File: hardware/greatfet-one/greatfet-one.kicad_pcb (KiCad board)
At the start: 4 copper layers, 70.6 x 53.3 mm, 88 parts, among them J1 NEIGHBOR1, J2 NEIGHBOR2, J3 USB-MICRO-B-SHIELDED, J4 USB-MICRO-B-SHIELDED, J5 JTAG, J7 BONUS_ROW, SW1 DFU, SW2 RESET, U1 LPC4330FBD144, U2 W25Q16DV, U3 AP7333, U4 IP4220CZ6, U5 NX5P2553GV, X1 XTAL4PIN, X2 RTC_XTAL

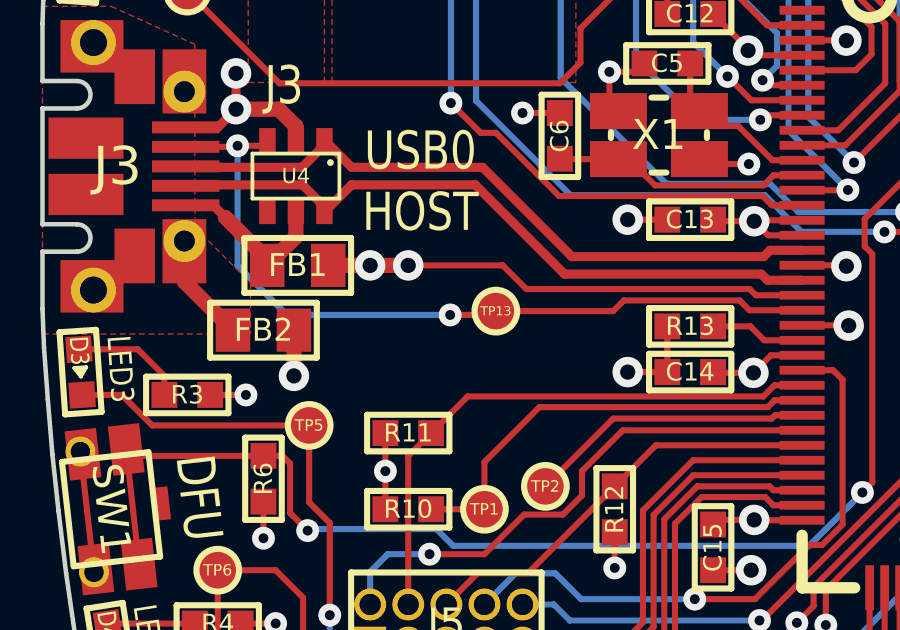
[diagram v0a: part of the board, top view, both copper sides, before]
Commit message: GreatFET One: updated layout to reflect VBUS changes
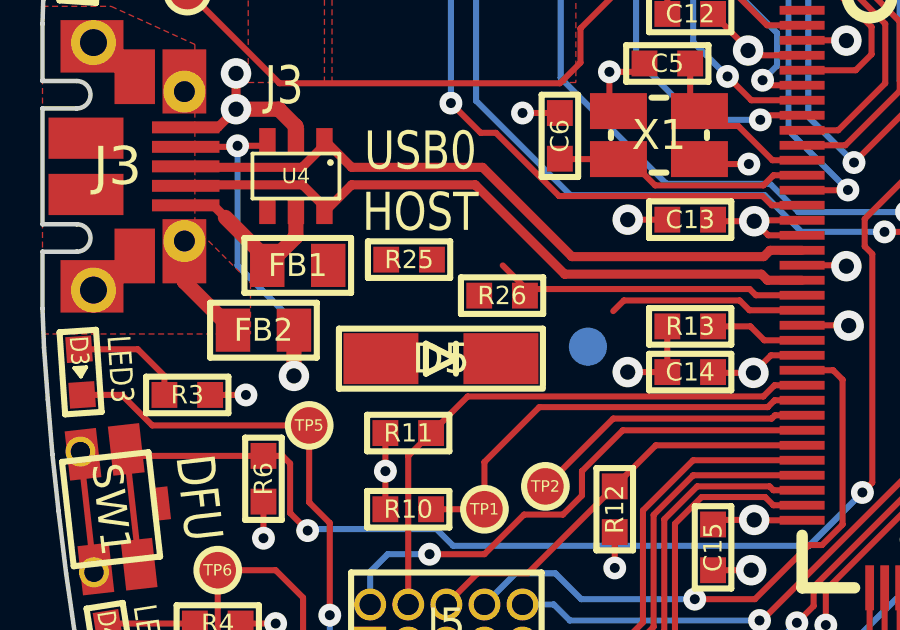
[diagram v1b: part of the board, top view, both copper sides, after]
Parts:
- added D5: VBUS_DIODE, gsg-modules:B140-13-F, F.Cu at (119.2, 104.2)
- added R25: 10k, gsg-modules:0603, F.Cu at (118.1, 100.9)
- added R26: 18k, gsg-modules:0603, F.Cu at (121.2, 102.1)
- R22: value 12.0k -> 18k
- TP13: moved to B.Cu
- X1: value XTAL4PIN -> MCU_XTAL
- moved TP13 3.29 mm to (124.1, 103.8)
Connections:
- net Net-(FB1-Pad1) renamed /USB0_VBUS
- C10 pad 1: /VBUS -> +5V
- C4 pad 1: /VBUS -> +5V
- FB1 pad 2: /VBUS -> Net-(D5-Pad2)
- J2 pad 2: /VBUS -> +5V
- U1 pad 21: /VBUS -> /USB0_SENSE
- U3 pad 1: /VBUS -> +5V
- U5 pad 1: /VBUS -> +5V
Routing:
- net /VBUS: track 21.2 -> 0.00 mm, vias 5 -> 0
- net /USB0_ID: track 26.6 -> 15.7 mm, vias 2 -> 1
- net /USB0_SENSE: track 0.00 -> 10.4 mm
- net +5V: track 0.00 -> 5.05 mm, vias 0 -> 3
- added copper zone on B.Cu, net +5V
- added copper zone on F.Cu, net +5V
- removed copper zone on B.Cu, net /VBUS
- removed copper zone on F.Cu, net /VBUS

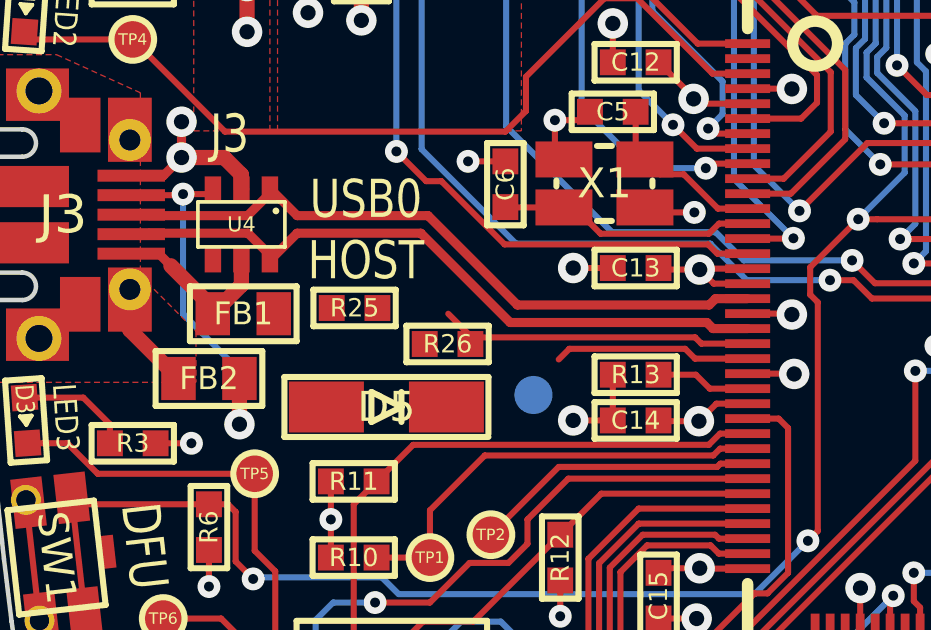
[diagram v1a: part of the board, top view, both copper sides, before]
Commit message: GreatFET One: changed U5 from NX5P2553GVH (end of life) to AP2553W6-7, updated ILIM resistor R23
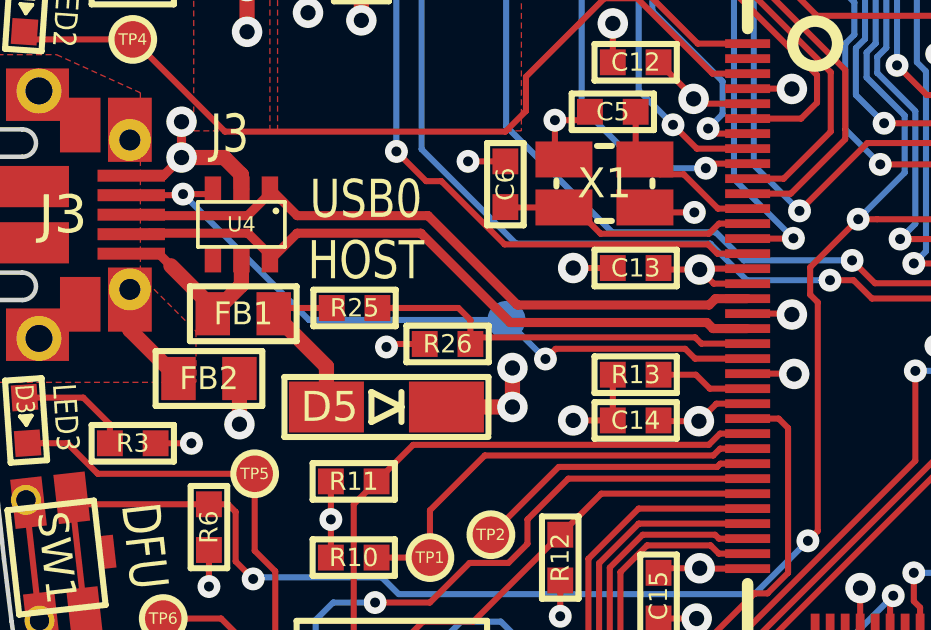
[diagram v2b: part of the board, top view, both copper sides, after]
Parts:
- R23: value 49.9k -> 43.2k
- U5: value NX5P2553GV -> AP2553W6-7
- moved TP13 2.66 mm to (123.2, 101.3)
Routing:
- net /USB0_ID: track 15.7 -> 24.2 mm, vias 1 -> 2
- net Net-(D5-Pad2): track 0.00 -> 5.85 mm
- net +5V: track 5.05 -> 8.55 mm, vias 3 -> 5
- net /USB0_SENSE: track 10.4 -> 13.5 mm
- net GND: track 80.9 -> 82.2 mm, vias 46 -> 47
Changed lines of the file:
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@@
   (general
     (links 356)
-    (no_connects 10)
-    (area 93.271704 68.58 207.466001 199.465001)
+    (no_connects 0)
+    (area 105.842999 71.044999 176.605001 124.535001)
     (thickness 1.6)
     (drawings 154)
-    (tracks 1422)
+    (tracks 1438)
     (zones 0)
     (modules 91)
@@
       (effects (font (size 0.508 0.508) (thickness 0.127)))
     )
-    (fp_text value NX5P2553GV (at 0 0 180) (layer F.SilkS) hide
+    (fp_text value AP2553W6-7 (at 0 0 180) (layer F.SilkS) hide
       (effects (font (size 0.762 0.889) (thickness 0.1905)))
     )
@@
       (effects (font (size 0.6096 0.6096) (thickness 0.1524)))
     )
-    (fp_text value 49.9k (at 0 0) (layer F.SilkS) hide
+    (fp_text value 43.2k (at 0 0) (layer F.SilkS) hide
       (effects (font (size 0.6096 0.6096) (thickness 0.1524)))
     )
@@
   )
   (module gsg-modules:TESTPOINT-50MIL (layer B.Cu)
-    (at 124.1 103.8)
+    (at 123.2 101.3)
     (fp_text reference TP13 (at 0 0) (layer B.SilkS)
       (effects (font (size 0.3048 0.3048) (thickness 0.0762)) (justify mirror))
@@
   (module gsg-modules:B140-13-F placed (layer F.Cu)
     (at 119.2 104.2 180)
-    (fp_text reference D5 (at 0 0 360) (layer F.SilkS)
+    (fp_text reference D5 (at 1.9 0 360) (layer F.SilkS)
       (effects (font (size 1 1) (thickness 0.15)))
     )
@@
   (gr_line (start 172.72 124.46) (end 112.3188 124.46) (angle 90) (layer Edge.Cuts) (width 0.15))
   (gr_line (start 112.3188 71.12) (end 172.72 71.12) (angle 90) (layer Edge.Cuts) (width 0.15))
+  (segment (start 120.476 102.1) (end 119.3 102.1) (width 0.2032) (layer F.Cu) (net 1))
+  (via (at 119.2 102.2) (size 0.762) (drill 0.3302) (layers F.Cu B.Cu) (net 1))
+  (segment (start 119.3 102.1) (end 119.2 102.2) (width 0.2032) (layer F.Cu) (net 1))
   (segment (start 123.1646 96.012) (end 121.92 96.012) (width 0.2032) (layer F.Cu) (net 1))
   (via (at 121.92 96.012) (size 0.762) (drill 0.3302) (layers F.Cu B.Cu) (net 1))
@@
   (segment (start 167.894 75.184) (end 167.894 76.708) (width 0.2032) (layer F.Cu) (net 91))
   (segment (start 166.37 73.66) (end 167.894 75.184) (width 0.2032) (layer F.Cu) (net 91) (status 10))
-  (segment (start 125.2982 102.2604) (end 124.9426 102.616) (width 0.2032) (layer F.Cu) (net 92))
-  (segment (start 129.159 102.2604) (end 125.2982 102.2604) (width 0.2032) (layer F.Cu) (net 92))
-  (segment (start 129.48666 102.58806) (end 129.159 102.2604) (width 0.2032) (layer F.Cu) (net 92))
+  (segment (start 116.6162 101.3) (end 112.4204 97.1042) (width 0.2032) (layer B.Cu) (net 92))
+  (segment (start 129.159 102.2604) (end 124.8396 102.2604) (width 0.2032) (layer F.Cu) (net 92))
   (segment (start 131.23926 102.58806) (end 129.48666 102.58806) (width 0.2032) (layer F.Cu) (net 92))
-  (segment (start 114.061238 102.743) (end 112.4204 101.102162) (width 0.2032) (layer B.Cu) (net 92))
+  (segment (start 129.48666 102.58806) (end 129.159 102.2604) (width 0.2032) (layer F.Cu) (net 92))
+  (segment (start 123.2 101.3) (end 116.6162 101.3) (width 0.2032) (layer B.Cu) (net 92))
+  (segment (start 124.5 102.6) (end 123.2 101.3) (width 0.2032) (layer B.Cu) (net 92))
+  (via (at 124.5 102.6) (size 0.762) (drill 0.3302) (layers F.Cu B.Cu) (net 92))
+  (segment (start 124.8396 102.2604) (end 124.5 102.6) (width 0.2032) (layer F.Cu) (net 92))
   (via (at 112.4204 97.1042) (size 0.762) (drill 0.3302) (layers F.Cu B.Cu) (net 92))
-  (segment (start 112.4204 101.102162) (end 112.4204 97.1042) (width 0.2032) (layer B.Cu) (net 92))
   (segment (start 113.2258 97.1042) (end 112.4204 97.1042) (width 0.2032) (layer F.Cu) (net 92))
   (segment (start 112.3846 97.14) (end 112.4204 97.1042) (width 0.2032) (layer F.Cu) (net 92))
@@
   (segment (start 170.688 103.759) (end 172.657 101.79) (width 0.508) (layer F.Cu) (net 136))
   (segment (start 172.657 101.79) (end 172.9924 101.79) (width 0.508) (layer F.Cu) (net 136))
+  (segment (start 123.4 102.9) (end 123.4 104.2) (width 0.508) (layer F.Cu) (net 137))
+  (segment (start 123.4 104.2) (end 121.2 104.2) (width 0.508) (layer F.Cu) (net 137))
+  (via (at 123.4 104.2) (size 1.016) (drill 0.508) (layers F.Cu B.Cu) (net 137))
+  (via (at 123.4 102.9) (size 1.016) (drill 0.508) (layers F.Cu B.Cu) (net 137))
   (segment (start 116.586 89.789) (end 116.586 91.059) (width 0.508) (layer F.Cu) (net 137))
   (via (at 116.586 91.059) (size 1.016) (drill 0.508) (layers F.Cu B.Cu) (net 137))
@@
   (segment (start 171.13 86.426) (end 171.196 86.36) (width 0.3048) (layer F.Cu) (net 137))
   (via (at 171.196 86.36) (size 1.016) (drill 0.508) (layers F.Cu B.Cu) (net 137))
+  (segment (start 117.2 104.2) (end 117.2 102.849) (width 0.508) (layer F.Cu) (net 138))
+  (segment (start 117.2 102.849) (end 115.443 101.092) (width 0.508) (layer F.Cu) (net 138))
+  (segment (start 117.376 100.9) (end 115.635 100.9) (width 0.2032) (layer F.Cu) (net 138))
+  (segment (start 115.635 100.9) (end 115.443 101.092) (width 0.2032) (layer F.Cu) (net 138))
   (segment (start 113.411 100.8888) (end 113.411 101.092) (width 0.508) (layer F.Cu) (net 139))
   (segment (start 113.411 100.8888) (end 112.014 99.4918) (width 0.508) (layer F.Cu) (net 139))
@@
   (segment (start 113.411 101.092) (end 114.366 100.137) (width 0.508) (layer F.Cu) (net 139))
   (segment (start 114.366 100.137) (end 114.366 99.314) (width 0.508) (layer F.Cu) (net 139))
-  (segment (start 122.047 101.8794) (end 121.2596 101.092) (width 0.2032) (layer F.Cu) (net 140))
-  (segment (start 129.4892 101.8794) (end 122.047 101.8794) (width 0.2032) (layer F.Cu) (net 140))
+  (segment (start 122.2206 101.8794) (end 122 102.1) (width 0.2032) (layer F.Cu) (net 140))
+  (segment (start 118.9 100.9) (end 121.6 100.9) (width 0.2032) (layer F.Cu) (net 140))
+  (segment (start 122 101.3) (end 122 102.1) (width 0.2032) (layer F.Cu) (net 140))
+  (segment (start 121.6 100.9) (end 122 101.3) (width 0.2032) (layer F.Cu) (net 140))
+  (segment (start 122.2206 101.8794) (end 129.4892 101.8794) (width 0.2032) (layer F.Cu) (net 140))
+  (segment (start 129.69748 102.08768) (end 131.23926 102.08768) (width 0.2032) (layer F.Cu) (net 140))
   (segment (start 129.69748 102.08768) (end 129.4892 101.8794) (width 0.2032) (layer F.Cu) (net 140))
-  (segment (start 131.23926 102.08768) (end 129.69748 102.08768) (width 0.2032) (layer F.Cu) (net 140))
   (zone (net 1) (net_name GND) (layer C2.Cu) (hatch edge 0.508)
     (connect_pads (clearance 0.254))

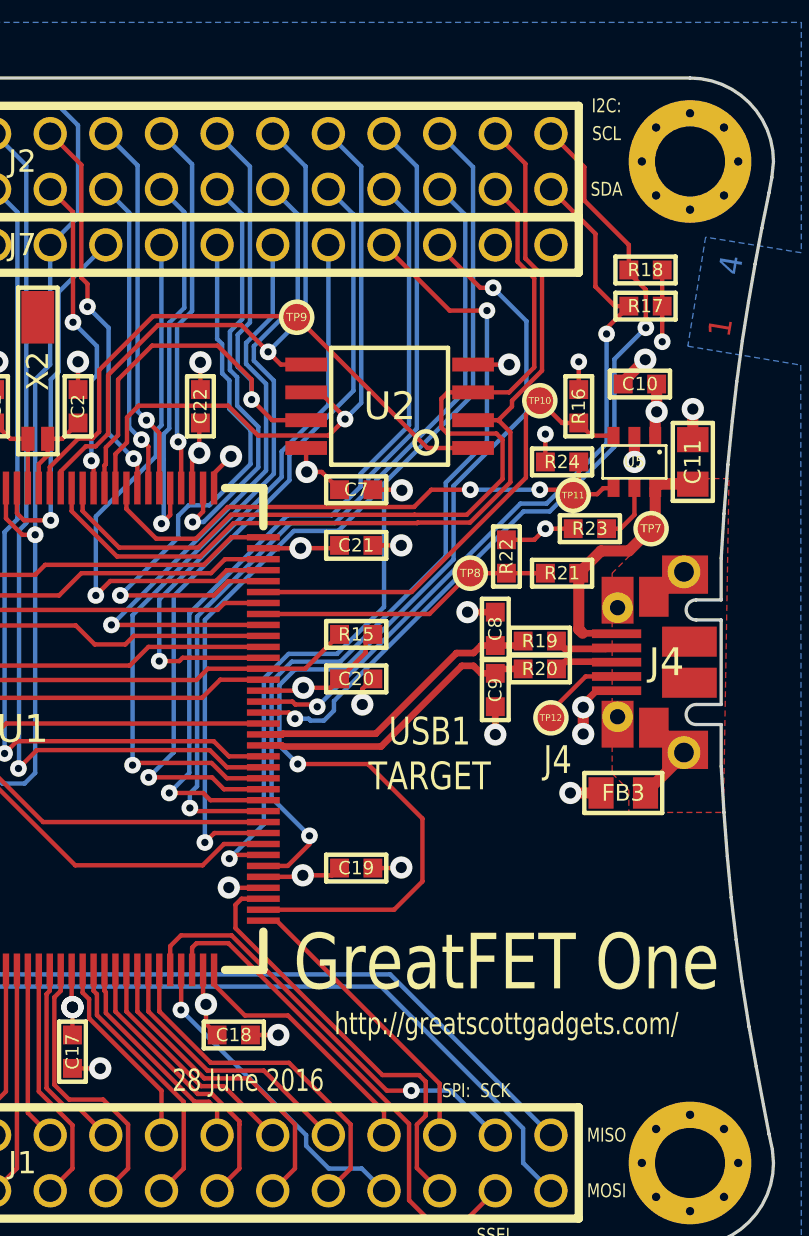
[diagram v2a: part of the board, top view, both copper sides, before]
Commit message: GreatFET One: moved R17 and R18 out of probable lever area
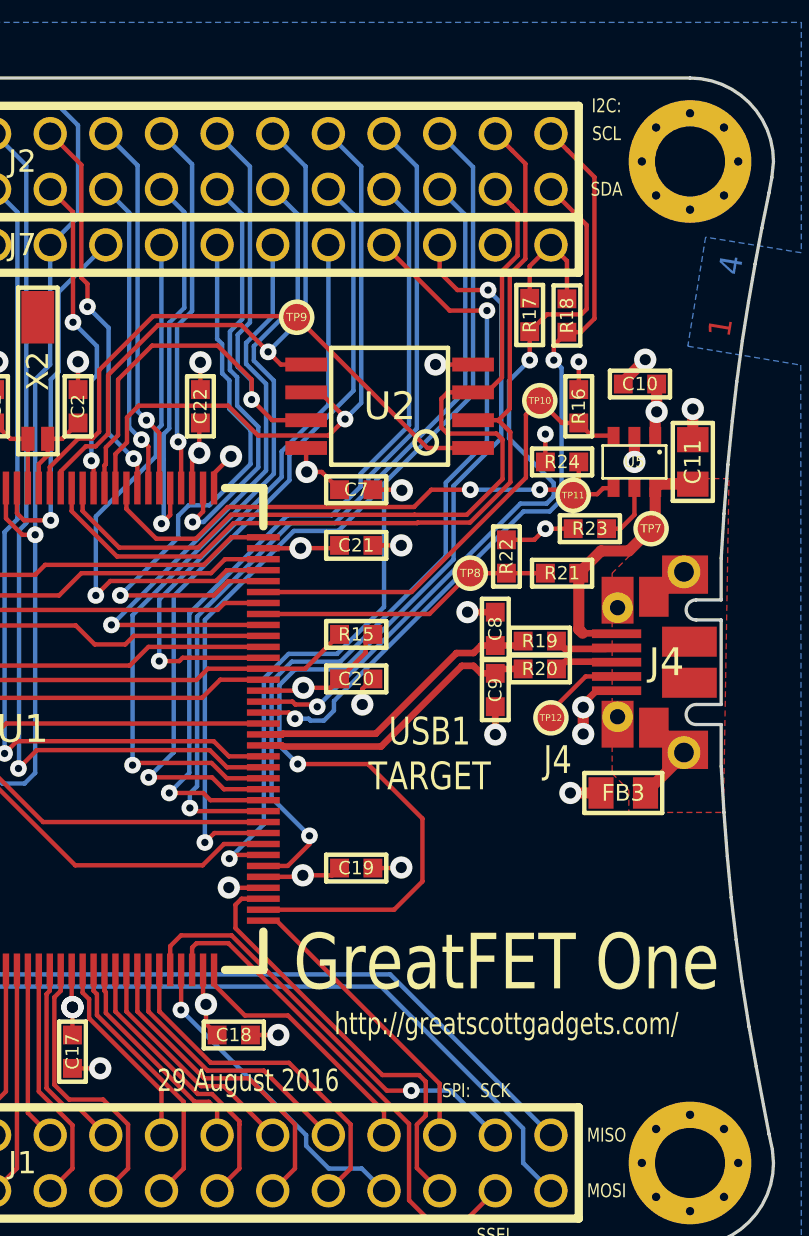
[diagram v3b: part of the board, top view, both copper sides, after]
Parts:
- moved R17 5.30 mm to (165.4, 81.9), turned to 270 degrees
- moved R18 4.15 mm to (167.1, 82.0), turned to 270 degrees
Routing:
- net VCC: track 86.7 -> 88.8 mm, vias 27 -> 26
- net /I2C0_SCL: track 38.3 -> 37.0 mm
- net /P3_5: track 42.0 -> 40.8 mm
- net /I2C0_SDA: track 34.6 -> 35.3 mm
- net /P3_6: track 42.3 -> 41.7 mm
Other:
- board text added: "29 August 2016"
- board text removed: "28 June 2016"

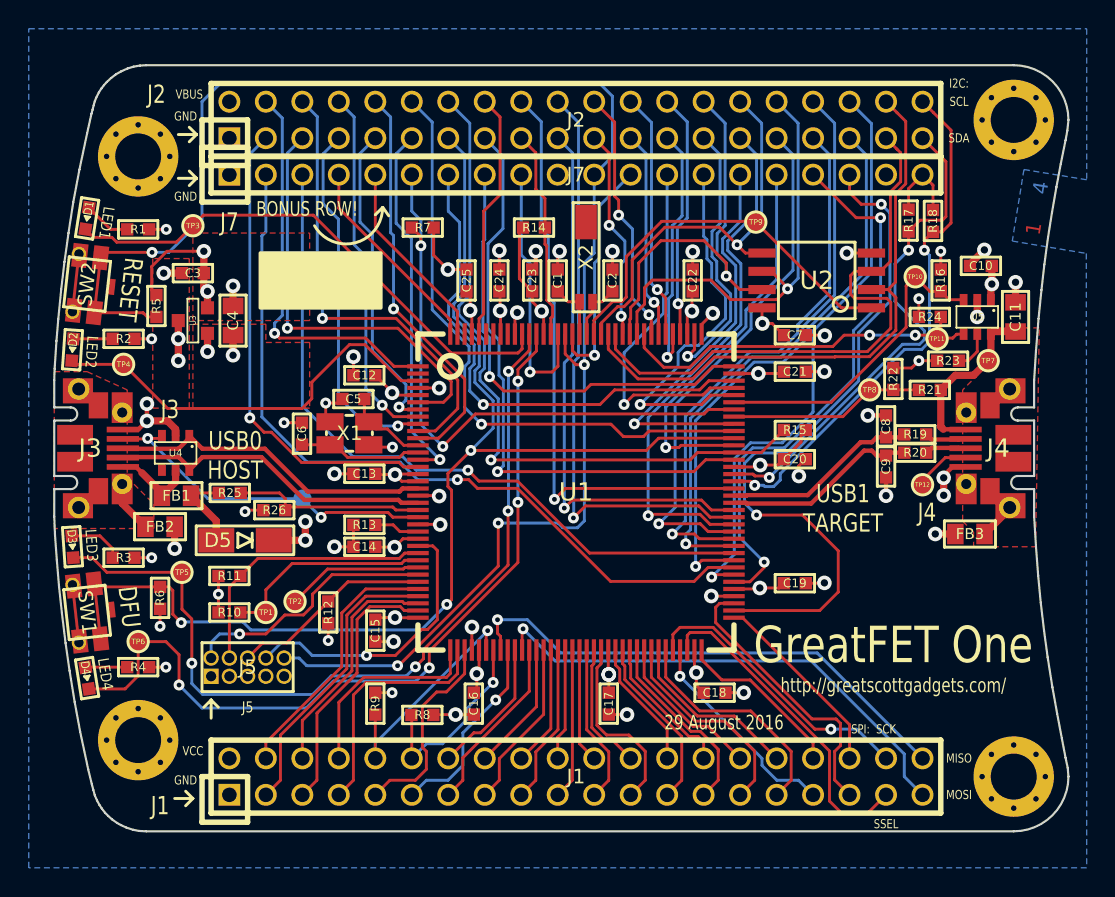
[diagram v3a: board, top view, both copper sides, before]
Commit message: GreatFET One: moved test points to bottom for manufacturing
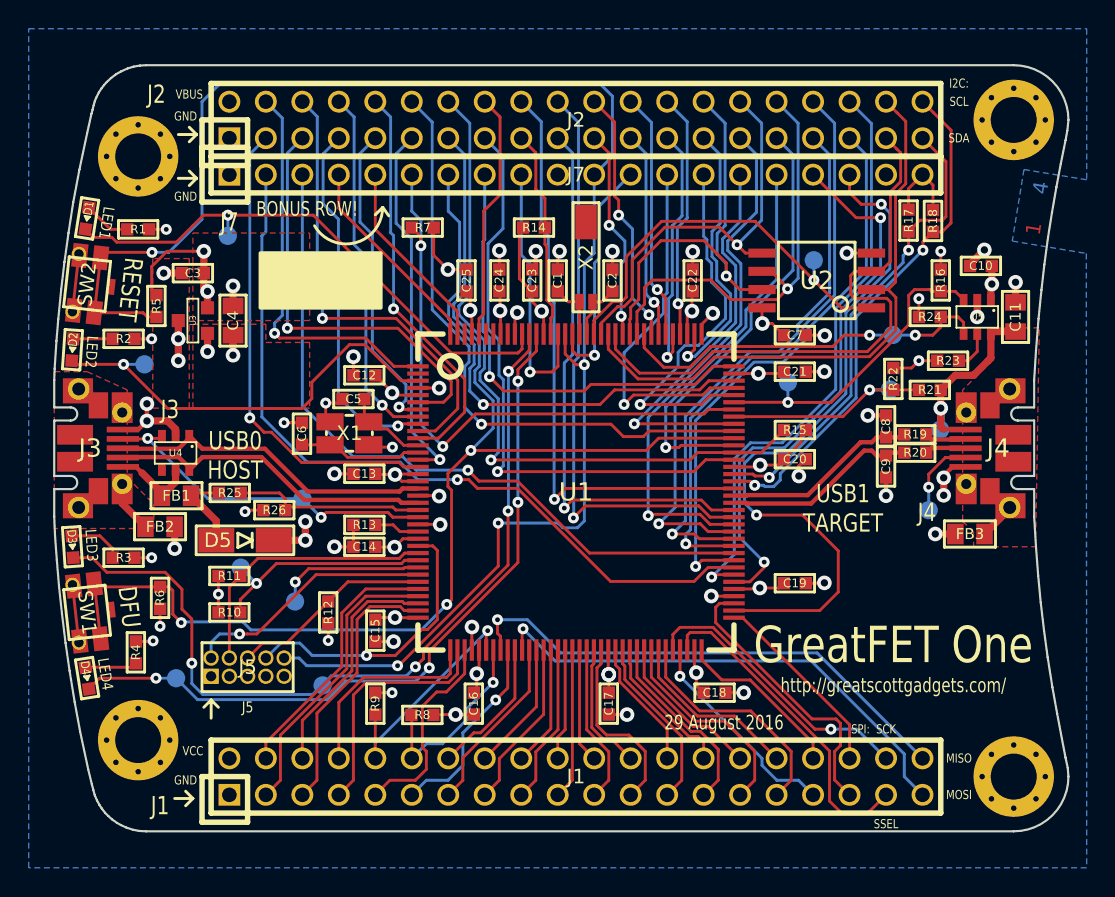
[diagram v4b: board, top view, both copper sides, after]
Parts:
- TP1, TP10, TP11, TP12, TP2, TP3, TP4, TP5, TP6, TP7, TP8, TP9: moved to B.Cu
- moved TP5 12.6 mm to (124.6, 114.3)
- moved TP10 11.5 mm to (157.0, 93.2)
- moved TP7 5.85 mm to (167.6, 96.5)
- moved TP9 4.83 mm to (158.8, 84.7)
- moved TP6 3.67 mm to (114.4, 113.8)
- moved TP1 3.58 mm to (118.9, 106.1)
- moved TP11 3.10 mm to (164.3, 89.9)
- moved TP3 2.53 mm to (118.0, 83.0)
- moved TP12 1.82 mm to (166.8, 102.1)
- moved TP4 1.46 mm to (112.2, 91.9)
- moved TP8 1.41 mm to (164.1, 93.7)
- moved R4 1.04 mm to (111.6, 112.0), turned to 270 degrees
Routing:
- net /LED4: track 57.1 -> 51.9 mm
- net /I2C0_SDA: track 35.3 -> 32.9 mm
- net /USB1_ID: track 3.96 -> 5.55 mm, vias 0 -> 1
- net /USB1_VBUS: track 12.2 -> 13.8 mm, vias 0 -> 1
- net /LED2: track 29.0 -> 30.5 mm, vias 0 -> 1
- net /LED1: track 36.7 -> 38.1 mm, vias 0 -> 1
- net /USB1_SENSE: track 13.6 -> 15.1 mm, vias 0 -> 1
- net /SPIFI_CS: track 27.3 -> 28.6 mm, vias 0 -> 1
- net /DBGEN: track 14.8 -> 15.9 mm, vias 0 -> 1
- net /I2C0_SCL: track 37.0 -> 36.0 mm
- net /TRST: track 9.54 -> 10.3 mm, vias 0 -> 1
- net Net-(D4-Pad2): track 2.92 -> 3.63 mm
- net /LED3: track 59.2 -> 58.5 mm
- net /USB1_EN: track 22.0 -> 22.1 mm, vias 0 -> 1
